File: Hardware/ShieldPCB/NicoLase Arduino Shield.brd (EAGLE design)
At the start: 54.3 x 62.2 mm, 21 parts, among them IC1 4050D, J1 ARDUINO_R3_SHIELD, U1 7432SE

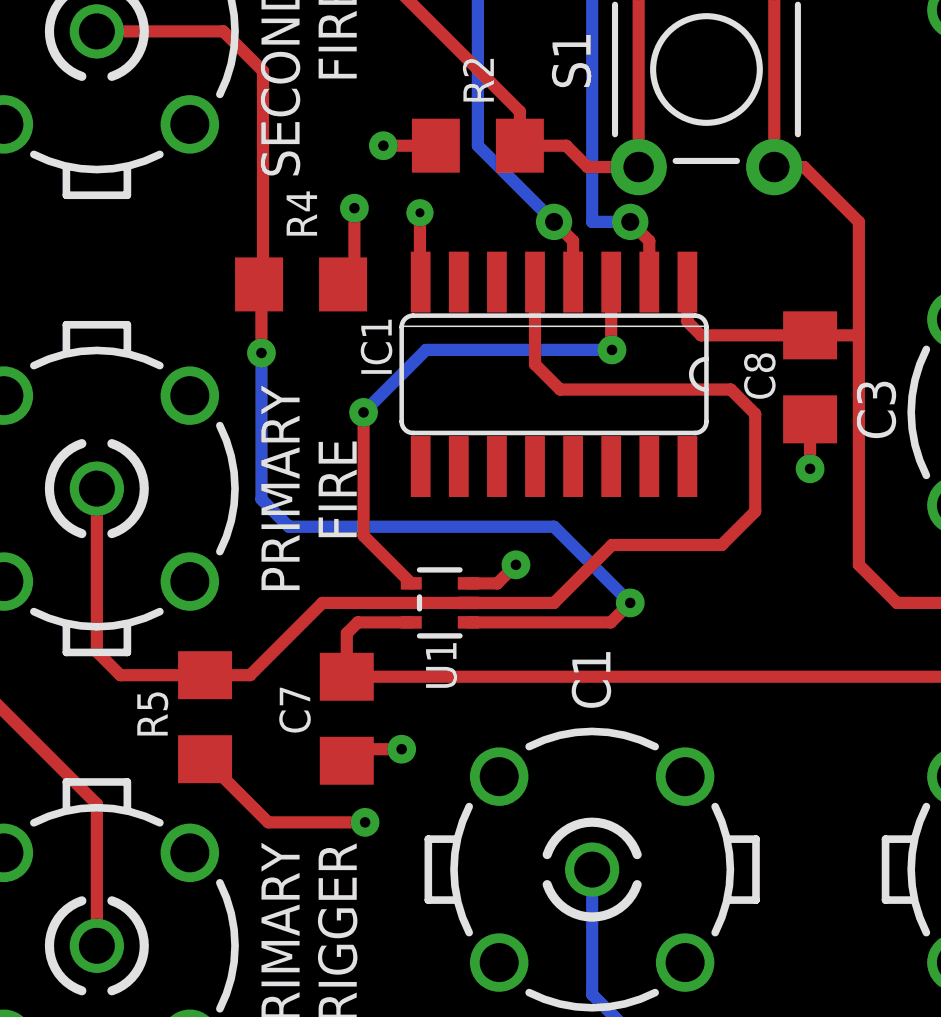
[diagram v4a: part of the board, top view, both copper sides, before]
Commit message: Grounded the non-used gates.
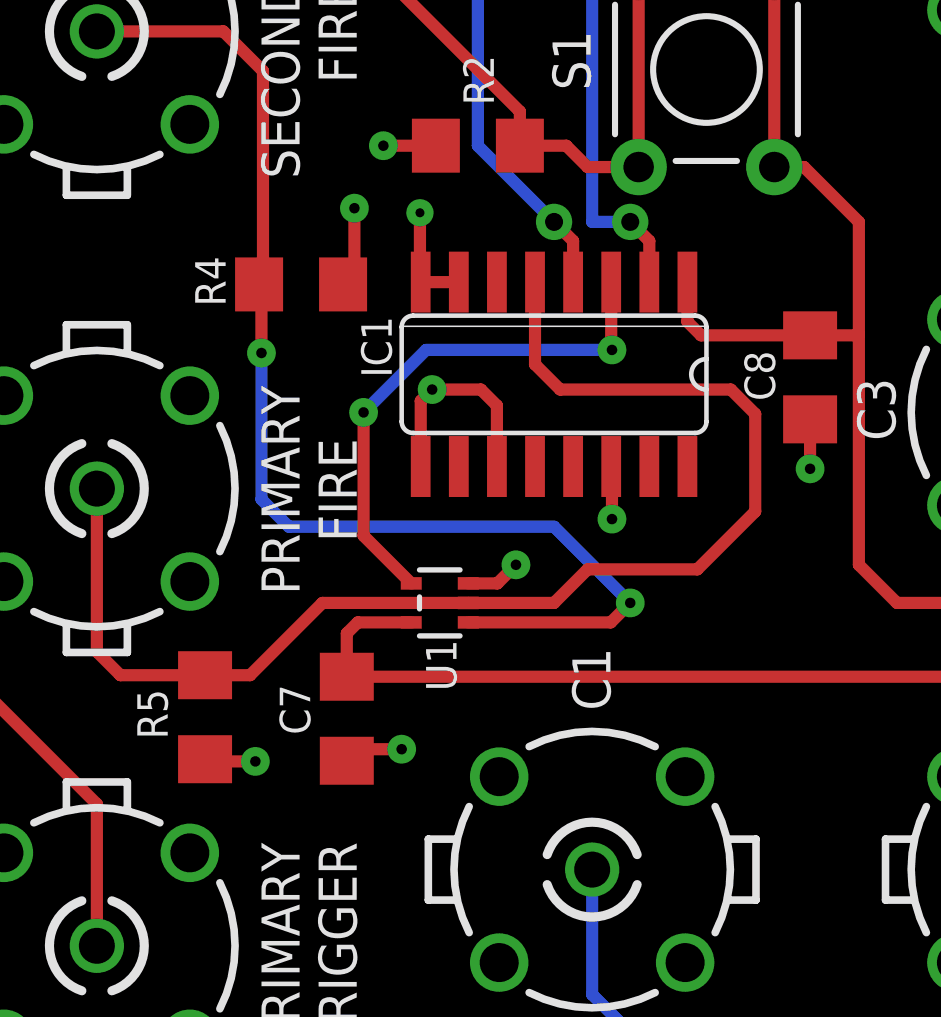
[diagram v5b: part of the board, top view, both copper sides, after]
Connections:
- net GND: now also IC1.11, IC1.14, IC1.7, IC1.9
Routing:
- net GND: track 21.1 -> 26.8 mm, vias 8 -> 10
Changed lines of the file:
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@@
 <?xml version="1.0" encoding="utf-8"?>
 <!DOCTYPE eagle SYSTEM "eagle.dtd">
-<eagle version="9.0.1">
+<eagle version="9.5.1">
 <drawing>
 <settings>
@@
 <param name="checkStop" value="0"/>
 <param name="checkValues" value="0"/>
+<param name="checkNames" value="1"/>
+<param name="checkWireStubs" value="1"/>
+<param name="checkPolygonWidth" value="0"/>
 <param name="useDiameter" value="13"/>
 <param name="maxErrors" value="50"/>
@@
 <element name="J1" library="SparkFun-Boards" package="UNO_R3_SHIELD" value="ARDUINO_R3_SHIELD" x="3.81" y="2.54" smashed="yes"/>
 <element name="R4" library="SparkFun-Resistors" package="1206" value="10k" x="22.0472" y="36.0172" smashed="yes" rot="R180">
-<attribute name="NAME" x="21.5646" y="38.354" size="1.016" layer="25" font="vector" ratio="12" rot="R270" align="bottom-center"/>
+<attribute name="NAME" x="18.5166" y="36.1188" size="1.016" layer="25" font="vector" ratio="12" rot="R270" align="bottom-center"/>
 <attribute name="VALUE" x="23.4442" y="37.5412" size="0.4064" layer="27" rot="R180"/>
 </element>
@@
 <contactref element="IC1" pad="5"/>
 <contactref element="PRIMARYFIRE" pad="1"/>
-<wire x1="30.48" y1="25.4" x2="32.4104" y2="27.3304" width="0.4064" layer="1"/>
+<wire x1="30.48" y1="25.4" x2="31.5976" y2="26.5176" width="0.4064" layer="1"/>
 <wire x1="27.62" y1="25.4" x2="22.7584" y2="25.4" width="0.4064" layer="1"/>
 <wire x1="22.7584" y1="25.4" x2="20.3484" y2="22.99" width="0.4064" layer="1"/>
@@
 <wire x1="36.3728" y1="32.512" x2="37.1856" y2="31.6992" width="0.4064" layer="1"/>
 <wire x1="37.1856" y1="31.6992" x2="37.1856" y2="28.448" width="0.4064" layer="1"/>
-<wire x1="36.068" y1="27.3304" x2="32.4104" y2="27.3304" width="0.4064" layer="1"/>
+<wire x1="35.2552" y1="26.5176" x2="31.5976" y2="26.5176" width="0.4064" layer="1"/>
 <wire x1="29.845" y1="36.0934" x2="29.845" y2="33.3502" width="0.4064" layer="1"/>
 <wire x1="30.6832" y1="32.512" x2="36.3728" y2="32.512" width="0.4064" layer="1"/>
-<wire x1="37.1856" y1="28.448" x2="36.068" y2="27.3304" width="0.4064" layer="1"/>
+<wire x1="37.1856" y1="28.448" x2="35.2552" y2="26.5176" width="0.4064" layer="1"/>
 </signal>
 <signal name="GND">
@@
 <wire x1="26.54" y1="48.26" x2="24.9428" y2="48.26" width="0.4064" layer="1"/>
 <via x="24.9428" y="48.26" extent="1-16" drill="0.35"/>
-<wire x1="24.1808" y1="18.0848" x2="20.952" y2="18.0848" width="0.4064" layer="1"/>
-<wire x1="20.952" y1="18.0848" x2="18.8468" y2="20.19" width="0.4064" layer="1"/>
-<via x="24.1808" y="18.0848" extent="1-16" drill="0.35"/>
-<wire x1="26.035" y1="36.0934" x2="26.0096" y2="36.1188" width="0.4064" layer="1"/>
+<wire x1="20.5232" y1="20.1168" x2="18.92" y2="20.1168" width="0.4064" layer="1"/>
+<wire x1="18.92" y1="20.1168" x2="18.8468" y2="20.19" width="0.4064" layer="1"/>
+<via x="20.5232" y="20.1168" extent="1-16" drill="0.35"/>
 <wire x1="26.0096" y1="36.1188" x2="26.0096" y2="38.4048" width="0.4064" layer="1"/>
 <via x="26.0096" y="38.4048" extent="1-16" drill="0.3"/>
@@
 <wire x1="39.0144" y1="31.5184" x2="39.0144" y2="29.8704" width="0.4064" layer="1"/>
 <via x="39.0144" y="29.8704" extent="1-16" drill="0.35"/>
+<contactref element="IC1" pad="7"/>
+<contactref element="IC1" pad="9"/>
+<contactref element="IC1" pad="11"/>
+<contactref element="IC1" pad="14"/>
+<wire x1="27.305" y1="36.0934" x2="26.035" y2="36.0934" width="0.4064" layer="1"/>
+<wire x1="26.035" y1="36.0934" x2="26.0096" y2="36.1188" width="0.4064" layer="1"/>
+<wire x1="26.035" y1="29.9466" x2="26.035" y2="32.131" width="0.4064" layer="1"/>
+<wire x1="26.035" y1="32.131" x2="26.416" y2="32.512" width="0.4064" layer="1"/>
+<via x="26.416" y="32.512" extent="1-16" drill="0.35"/>
+<wire x1="28.575" y1="29.9466" x2="28.575" y2="31.9786" width="0.4064" layer="1"/>
+<wire x1="28.575" y1="31.9786" x2="28.0416" y2="32.512" width="0.4064" layer="1"/>
+<wire x1="28.0416" y1="32.512" x2="26.416" y2="32.512" width="0.4064" layer="1"/>
+<via x="32.4104" y="28.194" extent="1-16" drill="0.35"/>
+<wire x1="32.4104" y1="28.194" x2="32.4104" y2="29.9212" width="0.4064" layer="1"/>
+<wire x1="32.4104" y1="29.9212" x2="32.385" y2="29.9466" width="0.4064" layer="1"/>
 </signal>
 <signal name="N$3">
@@
 </signal>
 </signals>
+<mfgpreviewcolors>
+<mfgpreviewcolor name="soldermaskcolor" color="0xC8008000"/>
+<mfgpreviewcolor name="silkscreencolor" color="0xFFFEFEFE"/>
+<mfgpreviewcolor name="backgroundcolor" color="0xFF282828"/>
+<mfgpreviewcolor name="coppercolor" color="0xFFFFBF00"/>
+<mfgpreviewcolor name="substratecolor" color="0xFF786E46"/>
+</mfgpreviewcolors>
 </board>
 </drawing>
